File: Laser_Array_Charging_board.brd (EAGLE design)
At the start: 80 x 90 mm, 16 parts, among them X1 1751248, X2 1751264, X3 22-23-2031

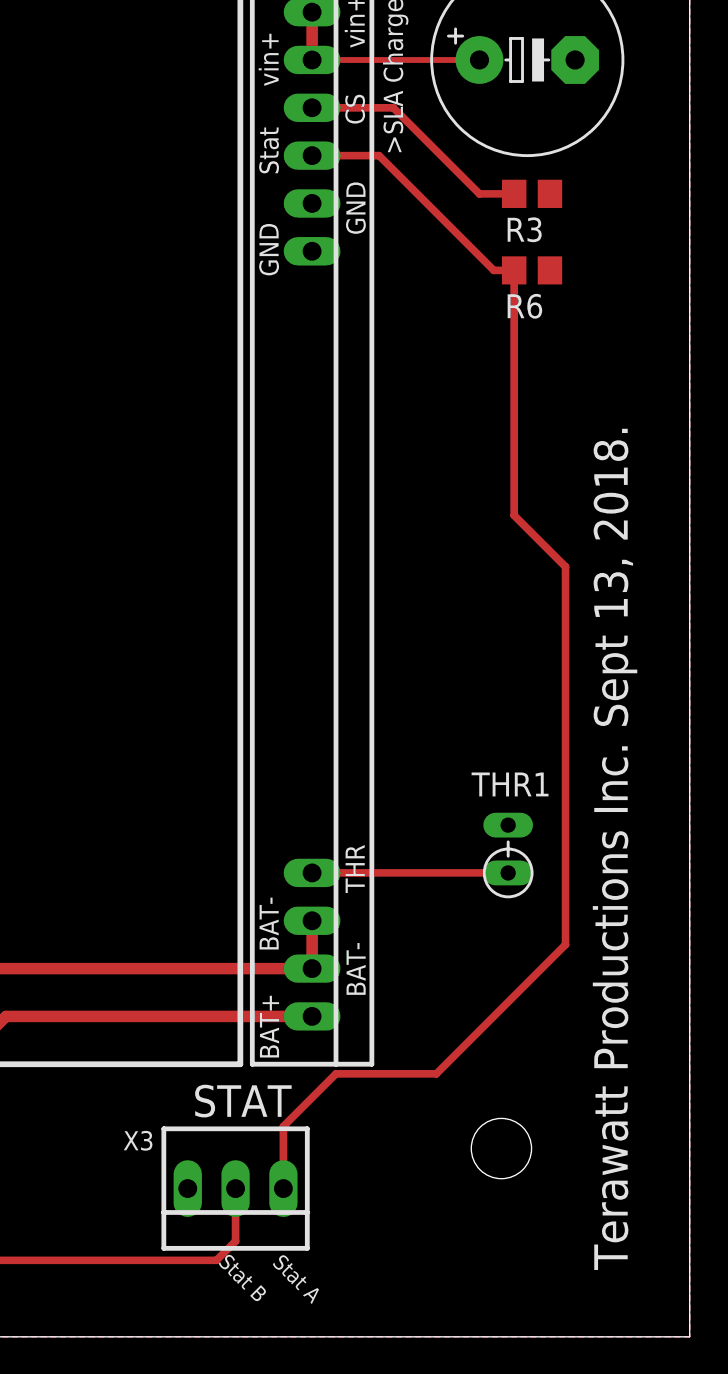
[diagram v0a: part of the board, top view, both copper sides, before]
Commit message: Temperature_Sensor board, changed traces from 14 to 16, V1.1
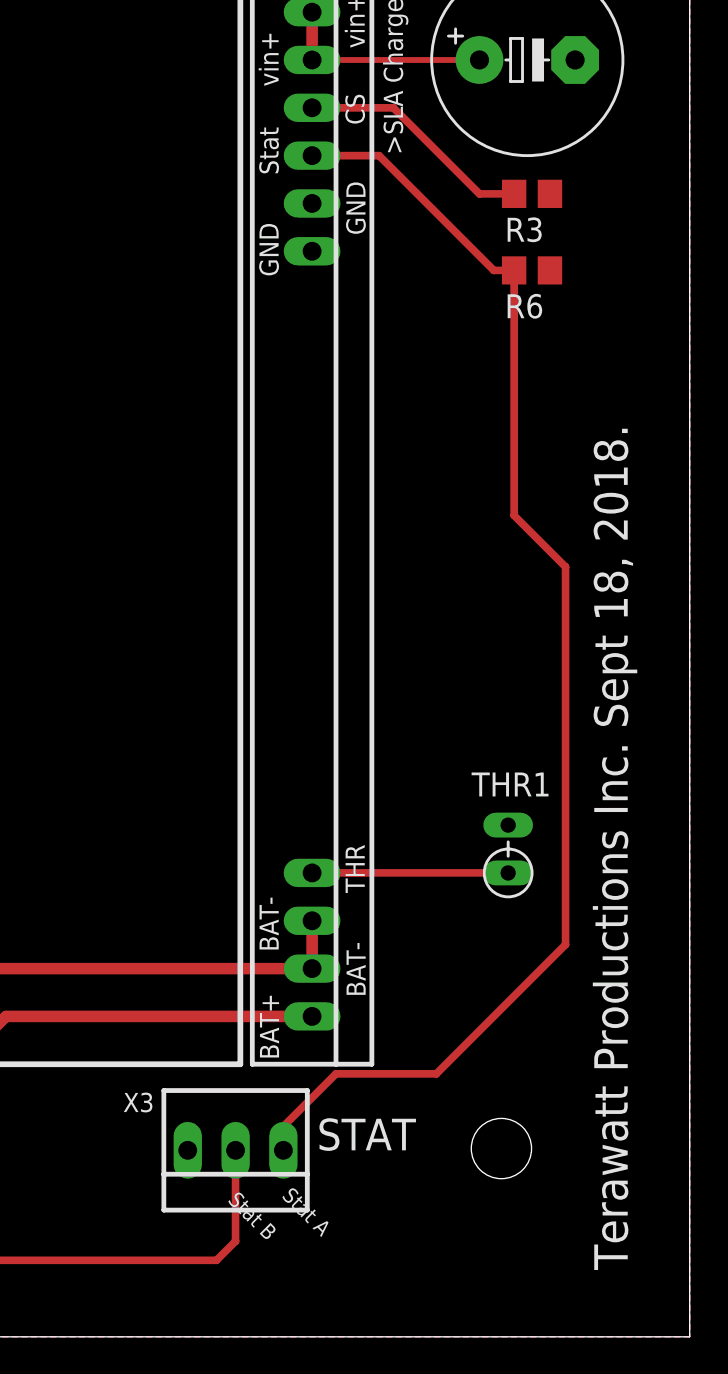
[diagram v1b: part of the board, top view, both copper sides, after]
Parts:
- moved X3 2.03 mm to (55.9, 9.91)
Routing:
- net STAT2: track 109.9 -> 112.0 mm
- net STAT1: track 72.5 -> 70.5 mm
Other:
- board text added: "Terawatt Productions Inc. Sept 18, 2018."
- board text removed: "Terawatt Productions Inc. Sept 13, 2018."
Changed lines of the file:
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@@
 <text x="54.864" y="72.644" size="1.778" layer="21">Unit A</text>
 <text x="17.018" y="72.39" size="1.778" layer="21">Unit B</text>
-<text x="57.785" y="3.8862" size="0.8128" layer="21" rot="R315">Stat A</text>
-<text x="54.9148" y="3.9116" size="0.8128" layer="21" rot="R315">Stat B</text>
+<text x="58.293" y="7.4422" size="0.8128" layer="21" rot="R315">Stat A</text>
+<text x="55.4228" y="7.2136" size="0.8128" layer="21" rot="R315">Stat B</text>
 <text x="33.528" y="3.556" size="0.8128" layer="21" rot="R315">BatA-</text>
 <text x="36.83" y="3.556" size="0.8128" layer="21" rot="R315">BatA+</text>
@@
 <text x="29.972" y="3.556" size="0.8128" layer="21" rot="R315">BatB+</text>
 <text x="28.702" y="12.446" size="1.6764" layer="21">BATTERY</text>
-<text x="53.594" y="11.684" size="1.6764" layer="21">STAT</text>
+<text x="60.198" y="9.906" size="1.6764" layer="21">STAT</text>
 <text x="50.8" y="75.946" size="1.6764" layer="21">POWER</text>
 <text x="4.318" y="18.034" size="1.778" layer="21" rot="R90">Battery Charger Board V1.0</text>
-<text x="76.708" y="3.556" size="1.778" layer="21" rot="R90">Terawatt Productions Inc. Sept 13, 2018.</text>
+<text x="76.708" y="3.556" size="1.778" layer="21" rot="R90">Terawatt Productions Inc. Sept 18, 2018.</text>
 <text x="49.276" y="86.614" size="1.143" layer="21">+12V</text>
 <text x="56.134" y="86.614" size="1.143" layer="21">GND</text>
@@
 <attribute name="NAME" x="50.759" y="79.4385" size="1.27" layer="25" rot="R90"/>
 </element>
-<element name="X3" library="Mine" package="22-23-2031" value="22-23-2031" x="55.88" y="7.874" smashed="yes" rot="R180">
-<attribute name="OC_FARNELL" value="1462950" x="55.88" y="7.874" size="1.778" layer="27" rot="R180" display="off"/>
-<attribute name="OC_NEWARK" value="30C0862" x="55.88" y="7.874" size="1.778" layer="27" rot="R180" display="off"/>
-<attribute name="MPN" value="22-23-2031" x="55.88" y="7.874" size="1.778" layer="27" rot="R180" display="off"/>
-<attribute name="MF" value="MOLEX" x="55.88" y="7.874" size="1.778" layer="27" rot="R180" display="off"/>
-<attribute name="NAME" x="51.562" y="10.922" size="1.016" layer="25" ratio="10" rot="R180"/>
+<element name="X3" library="Mine" package="22-23-2031" value="22-23-2031" x="55.88" y="9.906" smashed="yes" rot="R180">
+<attribute name="OC_FARNELL" value="1462950" x="55.88" y="9.906" size="1.778" layer="27" rot="R180" display="off"/>
+<attribute name="OC_NEWARK" value="30C0862" x="55.88" y="9.906" size="1.778" layer="27" rot="R180" display="off"/>
+<attribute name="MPN" value="22-23-2031" x="55.88" y="9.906" size="1.778" layer="27" rot="R180" display="off"/>
+<attribute name="MF" value="MOLEX" x="55.88" y="9.906" size="1.778" layer="27" rot="R180" display="off"/>
+<attribute name="NAME" x="51.562" y="12.954" size="1.016" layer="25" ratio="10" rot="R180"/>
 </element>
 <element name="CHG1" library="Mine" package="SLA_CHARGER" value="AG102_SLA_CHARGER" x="59.944" y="47.498" rot="R270"/>
@@
 <wire x1="63.5" y1="62.738" x2="69.596" y2="56.642" width="0.4064" layer="1"/>
 <wire x1="69.596" y1="56.642" x2="70.678" y2="56.642" width="0.4064" layer="1"/>
-<wire x1="58.42" y1="7.874" x2="58.42" y2="11.176" width="0.4064" layer="1"/>
-<wire x1="58.42" y1="11.176" x2="61.214" y2="13.97" width="0.4064" layer="1"/>
 <wire x1="61.214" y1="13.97" x2="66.548" y2="13.97" width="0.4064" layer="1"/>
 <wire x1="66.548" y1="13.97" x2="73.406" y2="20.828" width="0.4064" layer="1"/>
@@
 <wire x1="73.406" y1="40.894" x2="70.678" y2="43.622" width="0.4064" layer="1"/>
 <wire x1="70.678" y1="43.622" x2="70.678" y2="56.642" width="0.4064" layer="1"/>
+<wire x1="61.214" y1="13.97" x2="58.42" y2="11.176" width="0.4064" layer="1"/>
+<wire x1="58.42" y1="11.176" x2="58.42" y2="9.906" width="0.4064" layer="1"/>
 </signal>
 <signal name="STAT2">
@@
 <wire x1="11.176" y1="55.626" x2="18.288" y2="62.738" width="0.4064" layer="1"/>
 <wire x1="18.288" y1="62.738" x2="19.812" y2="62.738" width="0.4064" layer="1"/>
-<wire x1="55.88" y1="7.874" x2="55.88" y2="5.08" width="0.4064" layer="1"/>
-<wire x1="55.88" y1="5.08" x2="54.864" y2="4.064" width="0.4064" layer="1"/>
 <wire x1="54.864" y1="4.064" x2="22.606" y2="4.064" width="0.4064" layer="1"/>
 <wire x1="22.606" y1="4.064" x2="5.588" y2="21.082" width="0.4064" layer="1"/>
@@
 <wire x1="5.588" y1="32.512" x2="9.586" y2="36.51" width="0.4064" layer="1"/>
 <wire x1="9.586" y1="36.51" x2="9.586" y2="55.626" width="0.4064" layer="1"/>
+<wire x1="55.88" y1="9.906" x2="55.88" y2="5.08" width="0.4064" layer="1"/>
+<wire x1="55.88" y1="5.08" x2="54.864" y2="4.064" width="0.4064" layer="1"/>
 </signal>
 <signal name="GND">

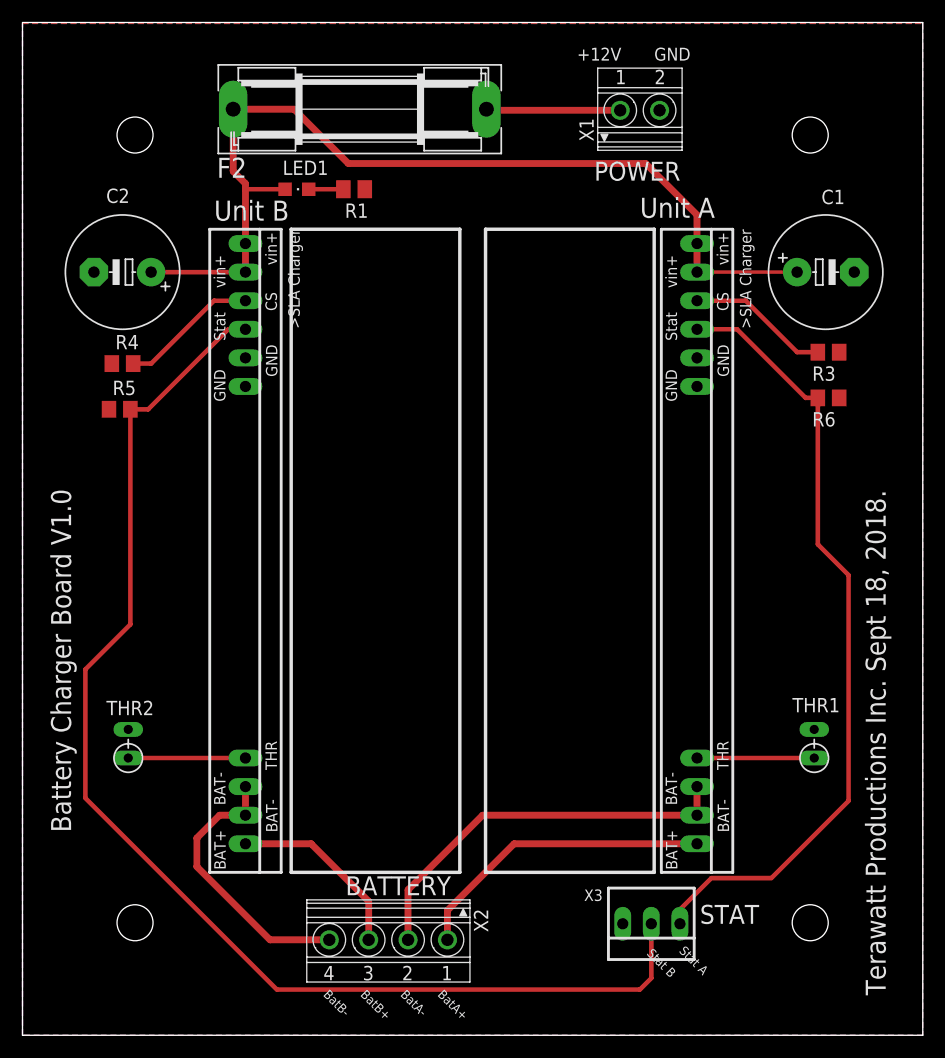
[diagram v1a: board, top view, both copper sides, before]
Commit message: Charging Board  header change, V1.1
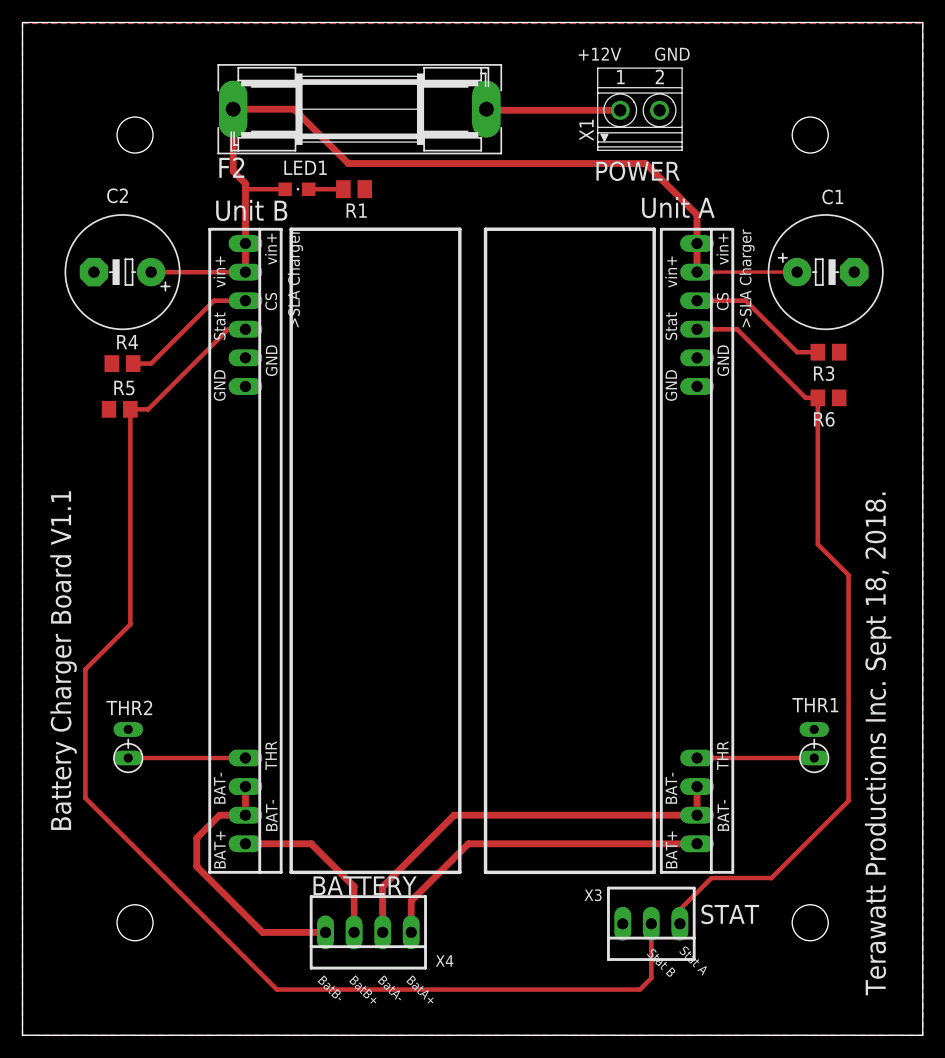
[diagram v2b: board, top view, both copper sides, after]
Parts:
- removed X2: 1751264, con-phoenix-350:1751264
- added X4: 22-23-2041, Mine:22-23-2041
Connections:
- net BATA_+: now also X4.1; no longer X2.1
- net BATA_-: now also X4.2; no longer X2.2
- net BATB_+: now also X4.3; no longer X2.3
- net BATB_-: now also X4.4; no longer X2.4
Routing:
- net BATA_+: track 27.2 -> 30.3 mm
- net BATA_-: track 35.4 -> 37.2 mm
- net BATB_+: track 16.5 -> 15.3 mm
- net BATB_-: track 24.7 -> 24.1 mm
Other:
- board text added: "Battery Charger Board V1.1"
- board text removed: "Battery Charger Board V1.0"
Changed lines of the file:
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@@
 <text x="58.293" y="7.4422" size="0.8128" layer="21" rot="R315">Stat A</text>
 <text x="55.4228" y="7.2136" size="0.8128" layer="21" rot="R315">Stat B</text>
-<text x="33.528" y="3.556" size="0.8128" layer="21" rot="R315">BatA-</text>
-<text x="36.83" y="3.556" size="0.8128" layer="21" rot="R315">BatA+</text>
-<text x="26.67" y="3.556" size="0.8128" layer="21" rot="R315">BatB-</text>
-<text x="29.972" y="3.556" size="0.8128" layer="21" rot="R315">BatB+</text>
-<text x="28.702" y="12.446" size="1.6764" layer="21">BATTERY</text>
+<text x="31.496" y="4.826" size="0.8128" layer="21" rot="R315">BatA-</text>
+<text x="34.036" y="4.826" size="0.8128" layer="21" rot="R315">BatA+</text>
+<text x="26.162" y="4.826" size="0.8128" layer="21" rot="R315">BatB-</text>
+<text x="28.956" y="4.826" size="0.8128" layer="21" rot="R315">BatB+</text>
+<text x="25.654" y="12.446" size="1.6764" layer="21">BATTERY</text>
 <text x="60.198" y="9.906" size="1.6764" layer="21">STAT</text>
 <text x="50.8" y="75.946" size="1.6764" layer="21">POWER</text>
-<text x="4.318" y="18.034" size="1.778" layer="21" rot="R90">Battery Charger Board V1.0</text>
+<text x="4.318" y="18.034" size="1.778" layer="21" rot="R90">Battery Charger Board V1.1</text>
 <text x="76.708" y="3.556" size="1.778" layer="21" rot="R90">Terawatt Productions Inc. Sept 18, 2018.</text>
 <text x="49.276" y="86.614" size="1.143" layer="21">+12V</text>
@@
 <attribute name="NAME" x="72.263" y="55.372" size="1.27" layer="25" rot="R180"/>
 </element>
-<element name="X2" library="con-phoenix-350" package="1751264" value="1751264" x="32.512" y="8.382" smashed="yes" rot="R180">
-<attribute name="OC_FARNELL" value="unknown" x="32.512" y="8.382" size="1.778" layer="27" rot="R180" display="off"/>
-<attribute name="OC_NEWARK" value="10R0934" x="32.512" y="8.382" size="1.778" layer="27" rot="R180" display="off"/>
-<attribute name="MPN" value="1751264" x="32.512" y="8.382" size="1.778" layer="27" rot="R180" display="off"/>
-<attribute name="MF" value="" x="32.512" y="8.382" size="1.778" layer="27" rot="R180" display="off"/>
-<attribute name="NAME" x="40.117" y="11.2395" size="1.27" layer="25" rot="R270"/>
-</element>
 <element name="X1" library="con-phoenix-350" package="1751248" value="1751248" x="54.864" y="82.296" smashed="yes">
 <attribute name="OC_FARNELL" value="unknown" x="54.864" y="82.296" size="1.778" layer="27" display="off"/>
@@
 <attribute name="NAME" x="30.734" y="73.914" size="1.27" layer="25" rot="R180"/>
 </element>
+<element name="X4" library="Mine" package="22-23-2041" value="22-23-2041" x="30.734" y="9.144" smashed="yes" rot="R180">
+<attribute name="MPN" value="22-23-2041" x="30.734" y="9.144" size="1.778" layer="27" rot="R180" display="off"/>
+<attribute name="OC_NEWARK" value="38C0355" x="30.734" y="9.144" size="1.778" layer="27" rot="R180" display="off"/>
+<attribute name="MF" value="MOLEX" x="30.734" y="9.144" size="1.778" layer="27" rot="R180" display="off"/>
+<attribute name="OC_FARNELL" value="1462920" x="30.734" y="9.144" size="1.778" layer="27" rot="R180" display="off"/>
+<attribute name="NAME" x="38.354" y="7.112" size="1.016" layer="25" ratio="10" rot="R180"/>
+</element>
 </elements>
 <signals>
 <signal name="BATA_-">
-<contactref element="X2" pad="2"/>
 <contactref element="CHG1" pad="20"/>
 <contactref element="CHG1" pad="22"/>
 <wire x1="59.944" y1="22.098" x2="59.944" y2="19.558" width="0.6096" layer="1"/>
-<wire x1="59.944" y1="19.558" x2="40.894" y2="19.558" width="0.6096" layer="1"/>
-<wire x1="40.894" y1="19.558" x2="34.262" y2="12.926" width="0.6096" layer="1"/>
-<wire x1="34.262" y1="12.926" x2="34.262" y2="8.482" width="0.6096" layer="1"/>
+<wire x1="59.944" y1="19.558" x2="38.354" y2="19.558" width="0.6096" layer="1"/>
+<contactref element="X4" pad="2"/>
+<wire x1="32.004" y1="9.144" x2="32.004" y2="13.208" width="0.6096" layer="1"/>
+<wire x1="32.004" y1="13.208" x2="38.354" y2="19.558" width="0.6096" layer="1"/>
 </signal>
 <signal name="VCC">
@@
 </signal>
 <signal name="BATA_+">
-<contactref element="X2" pad="1"/>
 <contactref element="CHG1" pad="23"/>
-<wire x1="59.944" y1="17.018" x2="43.688" y2="17.018" width="0.6096" layer="1"/>
-<wire x1="43.688" y1="17.018" x2="37.762" y2="11.092" width="0.6096" layer="1"/>
-<wire x1="37.762" y1="11.092" x2="37.762" y2="8.482" width="0.6096" layer="1"/>
+<wire x1="59.944" y1="17.018" x2="39.624" y2="17.018" width="0.6096" layer="1"/>
+<contactref element="X4" pad="1"/>
+<wire x1="34.544" y1="9.144" x2="34.544" y2="11.938" width="0.6096" layer="1"/>
+<wire x1="34.544" y1="11.938" x2="39.624" y2="17.018" width="0.6096" layer="1"/>
 </signal>
 <signal name="BATB_-">
-<contactref element="X2" pad="4"/>
 <contactref element="CHG2" pad="20"/>
 <contactref element="CHG2" pad="22"/>
@@
 <wire x1="17.526" y1="19.558" x2="15.494" y2="17.526" width="0.6096" layer="1"/>
 <wire x1="15.494" y1="17.526" x2="15.494" y2="14.986" width="0.6096" layer="1"/>
-<wire x1="15.494" y1="14.986" x2="21.998" y2="8.482" width="0.6096" layer="1"/>
-<wire x1="21.998" y1="8.482" x2="27.262" y2="8.482" width="0.6096" layer="1"/>
+<wire x1="15.494" y1="14.986" x2="21.336" y2="9.144" width="0.6096" layer="1"/>
+<contactref element="X4" pad="4"/>
+<wire x1="26.924" y1="9.144" x2="21.336" y2="9.144" width="0.6096" layer="1"/>
 </signal>
 <signal name="BATB_+">
 <contactref element="CHG2" pad="23"/>
-<contactref element="X2" pad="3"/>
 <wire x1="19.812" y1="17.018" x2="25.654" y2="17.018" width="0.6096" layer="1"/>
-<wire x1="25.654" y1="17.018" x2="30.762" y2="11.91" width="0.6096" layer="1"/>
-<wire x1="30.762" y1="11.91" x2="30.762" y2="8.482" width="0.6096" layer="1"/>
+<contactref element="X4" pad="3"/>
+<wire x1="29.464" y1="9.144" x2="29.464" y2="13.208" width="0.6096" layer="1"/>
+<wire x1="29.464" y1="13.208" x2="25.654" y2="17.018" width="0.6096" layer="1"/>
 </signal>
 <signal name="N$3">
